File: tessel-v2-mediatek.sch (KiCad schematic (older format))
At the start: 40 parts

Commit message: swapped in power labels
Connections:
- net labels added: +1.2V, +1.8V, +3.3V
- net labels removed: +1V2, +1V8, +3V3
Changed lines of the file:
@@
-	1    0    0    -1
-$EndComp
-$Comp
-L +1V2 #PWR?
-U 1 1 548FE6C6
-P 6450 5250
-F 0 "#PWR?" H 6450 5100 60  0001 C CNN
-F 1 "+1V2" H 6450 5390 60  0000 C CNN
-F 2 "" H 6450 5250 60  0000 C CNN
-F 3 "" H 6450 5250 60  0000 C CNN
-	1    6450 5250
-	1    0    0    -1
-$EndComp
-$Comp
-L +1V8 #PWR?
-U 1 1 548FEA98
-P 7550 5250
-F 0 "#PWR?" H 7550 5100 60  0001 C CNN
-F 1 "+1V8" H 7550 5390 60  0000 C CNN
-F 2 "" H 7550 5250 60  0000 C CNN
-F 3 "" H 7550 5250 60  0000 C CNN
-	1    7550 5250
 	1    0    0    -1
 $EndComp
@@
 $EndComp
 $Comp
-L +3V3 #PWR?
+L +3.3V #PWR?
 U 1 1 548FF520
 P 8500 5350
 F 0 "#PWR?" H 8500 5200 60  0001 C CNN
-F 1 "+3V3" H 8500 5490 60  0000 C CNN
+F 1 "+3.3V" H 8500 5490 60  0000 C CNN
 F 2 "" H 8500 5350 60  0000 C CNN
 F 3 "" H 8500 5350 60  0000 C CNN
@@
 $EndComp
 $Comp
-L +3V3 #PWR?
+L +3.3V #PWR?
 U 1 1 548FF90D
 P 9450 3850
 F 0 "#PWR?" H 9450 3700 60  0001 C CNN
-F 1 "+3V3" H 9450 3990 60  0000 C CNN
+F 1 "+3.3V" H 9450 3990 60  0000 C CNN
 F 2 "" H 9450 3850 60  0000 C CNN
 F 3 "" H 9450 3850 60  0000 C CNN
@@
 Connection ~ 11200 5650
 $Comp
-L +3V3 #PWR?
+L +3.3V #PWR?
 U 1 1 54901F95
 P 11200 5100
 F 0 "#PWR?" H 11200 4950 60  0001 C CNN
-F 1 "+3V3" H 11200 5240 60  0000 C CNN
+F 1 "+3.3V" H 11200 5240 60  0000 C CNN
 F 2 "" H 11200 5100 60  0000 C CNN
 F 3 "" H 11200 5100 60  0000 C CNN
@@
 Connection ~ 7000 8350
 $Comp
-L +3V3 #PWR?
+L +3.3V #PWR?
 U 1 1 54903A33
 P 6350 8250
 F 0 "#PWR?" H 6350 8100 60  0001 C CNN
-F 1 "+3V3" H 6350 8390 60  0000 C CNN
+F 1 "+3.3V" H 6350 8390 60  0000 C CNN
 F 2 "" H 6350 8250 60  0000 C CNN
 F 3 "" H 6350 8250 60  0000 C CNN
@@
 Connection ~ 5500 8850
 Connection ~ 5150 8850
-$Comp
-L +1V8 #PWR?
-U 1 1 549048D3
-P 4800 8200
-F 0 "#PWR?" H 4800 8050 60  0001 C CNN
-F 1 "+1V8" H 4800 8340 60  0000 C CNN
-F 2 "" H 4800 8200 60  0000 C CNN
-F 3 "" H 4800 8200 60  0000 C CNN
-	1    4800 8200
-	1    0    0    -1
-$EndComp
 Wire Wire Line
 	4800 8350 4800 8200
@@
 	2150 8300 2150 8400
 Connection ~ 2400 8300
-$Comp
-L +1V2 #PWR?
-U 1 1 54905795
-P 2750 8200
-F 0 "#PWR?" H 2750 8050 60  0001 C CNN
-F 1 "+1V2" H 2750 8340 60  0000 C CNN
-F 2 "" H 2750 8200 60  0000 C CNN
-F 3 "" H 2750 8200 60  0000 C CNN
-	1    2750 8200
-	1    0    0    -1
-$EndComp
 Wire Wire Line
 	2750 8200 2750 8300
@@
 	2150 8850 7250 8850
 Connection ~ 3750 8850
+$Comp
+L +1.2V #PWR?
+U 1 1 5490938C
+P 6450 5250
+F 0 "#PWR?" H 6450 5390 20  0001 C CNN
+F 1 "+1.2V" H 6450 5360 30  0000 C CNN
+F 2 "" H 6450 5250 60  0000 C CNN
+F 3 "" H 6450 5250 60  0000 C CNN
+	1    6450 5250
+	1    0    0    -1
+$EndComp
+$Comp
+L +1.8V #PWR?
+U 1 1 549093A0
+P 7550 5250
+F 0 "#PWR?" H 7550 5390 20  0001 C CNN
+F 1 "+1.8V" H 7550 5360 30  0000 C CNN
+F 2 "" H 7550 5250 60  0000 C CNN
+F 3 "" H 7550 5250 60  0000 C CNN
+	1    7550 5250
+	1    0    0    -1
+$EndComp
+$Comp
+L +1.8V #PWR?
+U 1 1 5490A3FA
+P 4800 8200
+F 0 "#PWR?" H 4800 8340 20  0001 C CNN
+F 1 "+1.8V" H 4800 8310 30  0000 C CNN
+F 2 "" H 4800 8200 60  0000 C CNN
+F 3 "" H 4800 8200 60  0000 C CNN
+	1    4800 8200
+	1    0    0    -1
+$EndComp
+$Comp
+L +1.2V #PWR?
+U 1 1 5490A9A8
+P 2750 8200
+F 0 "#PWR?" H 2750 8340 20  0001 C CNN
+F 1 "+1.2V" H 2750 8310 30  0000 C CNN
+F 2 "" H 2750 8200 60  0000 C CNN
+F 3 "" H 2750 8200 60  0000 C CNN
+	1    2750 8200
+	1    0    0    -1
+$EndComp
 $EndSCHEMATC

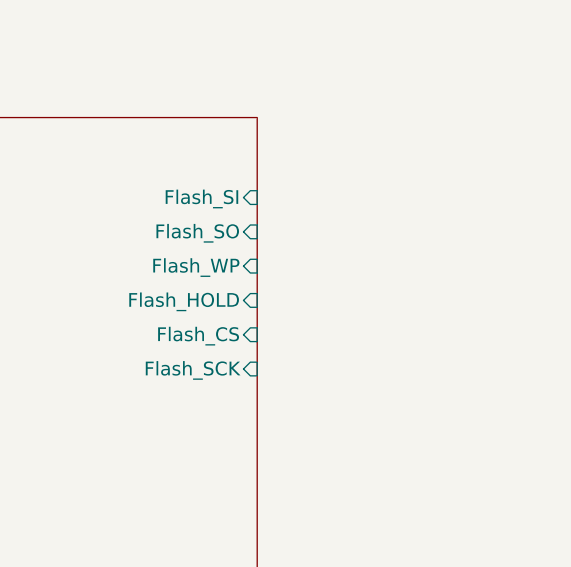
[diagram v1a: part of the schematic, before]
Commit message: adding mediatek flash labels
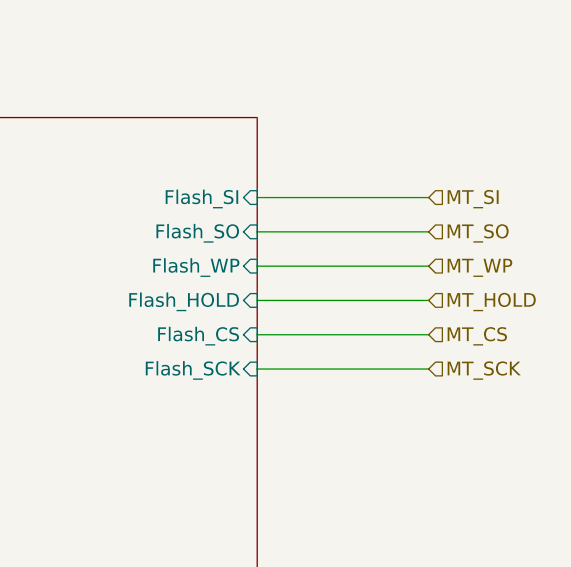
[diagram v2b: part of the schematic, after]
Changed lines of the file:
@@
 	1    0    0    -1
 $EndComp
+Text HLabel 19850 7450 2    60   Input ~ 0
+MT_SI
+Text HLabel 19850 7600 2    60   Input ~ 0
+MT_SO
+Text HLabel 19850 7750 2    60   Input ~ 0
+MT_WP
+Text HLabel 19850 7900 2    60   Input ~ 0
+MT_HOLD
+Text HLabel 19850 8050 2    60   Input ~ 0
+MT_CS
+Text HLabel 19850 8200 2    60   Input ~ 0
+MT_SCK
+Wire Wire Line
+	19100 7450 19850 7450
+Wire Wire Line
+	19100 7600 19850 7600
+Wire Wire Line
+	19100 7750 19850 7750
+Wire Wire Line
+	19100 7900 19850 7900
+Wire Wire Line
+	19100 8050 19850 8050
+Wire Wire Line
+	19100 8200 19850 8200
 $EndSCHEMATC

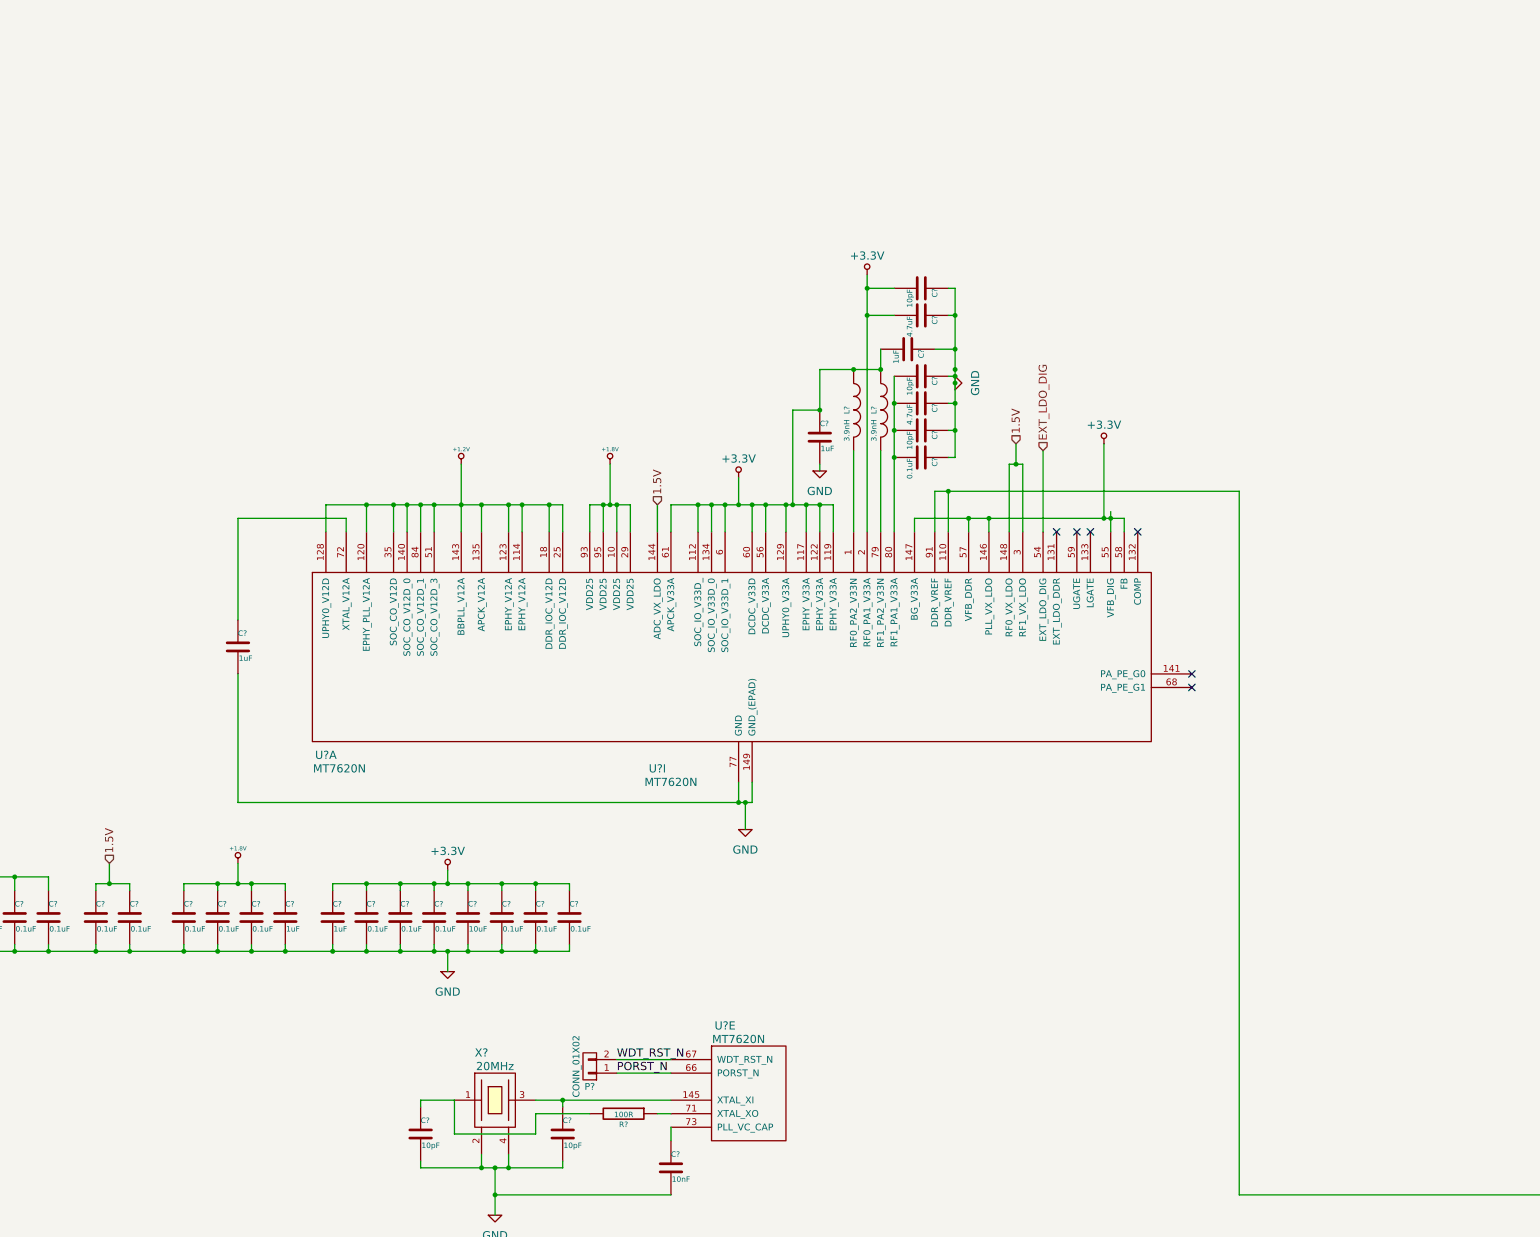
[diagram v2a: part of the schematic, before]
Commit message: cleaning up ram, rf, and mediatek power
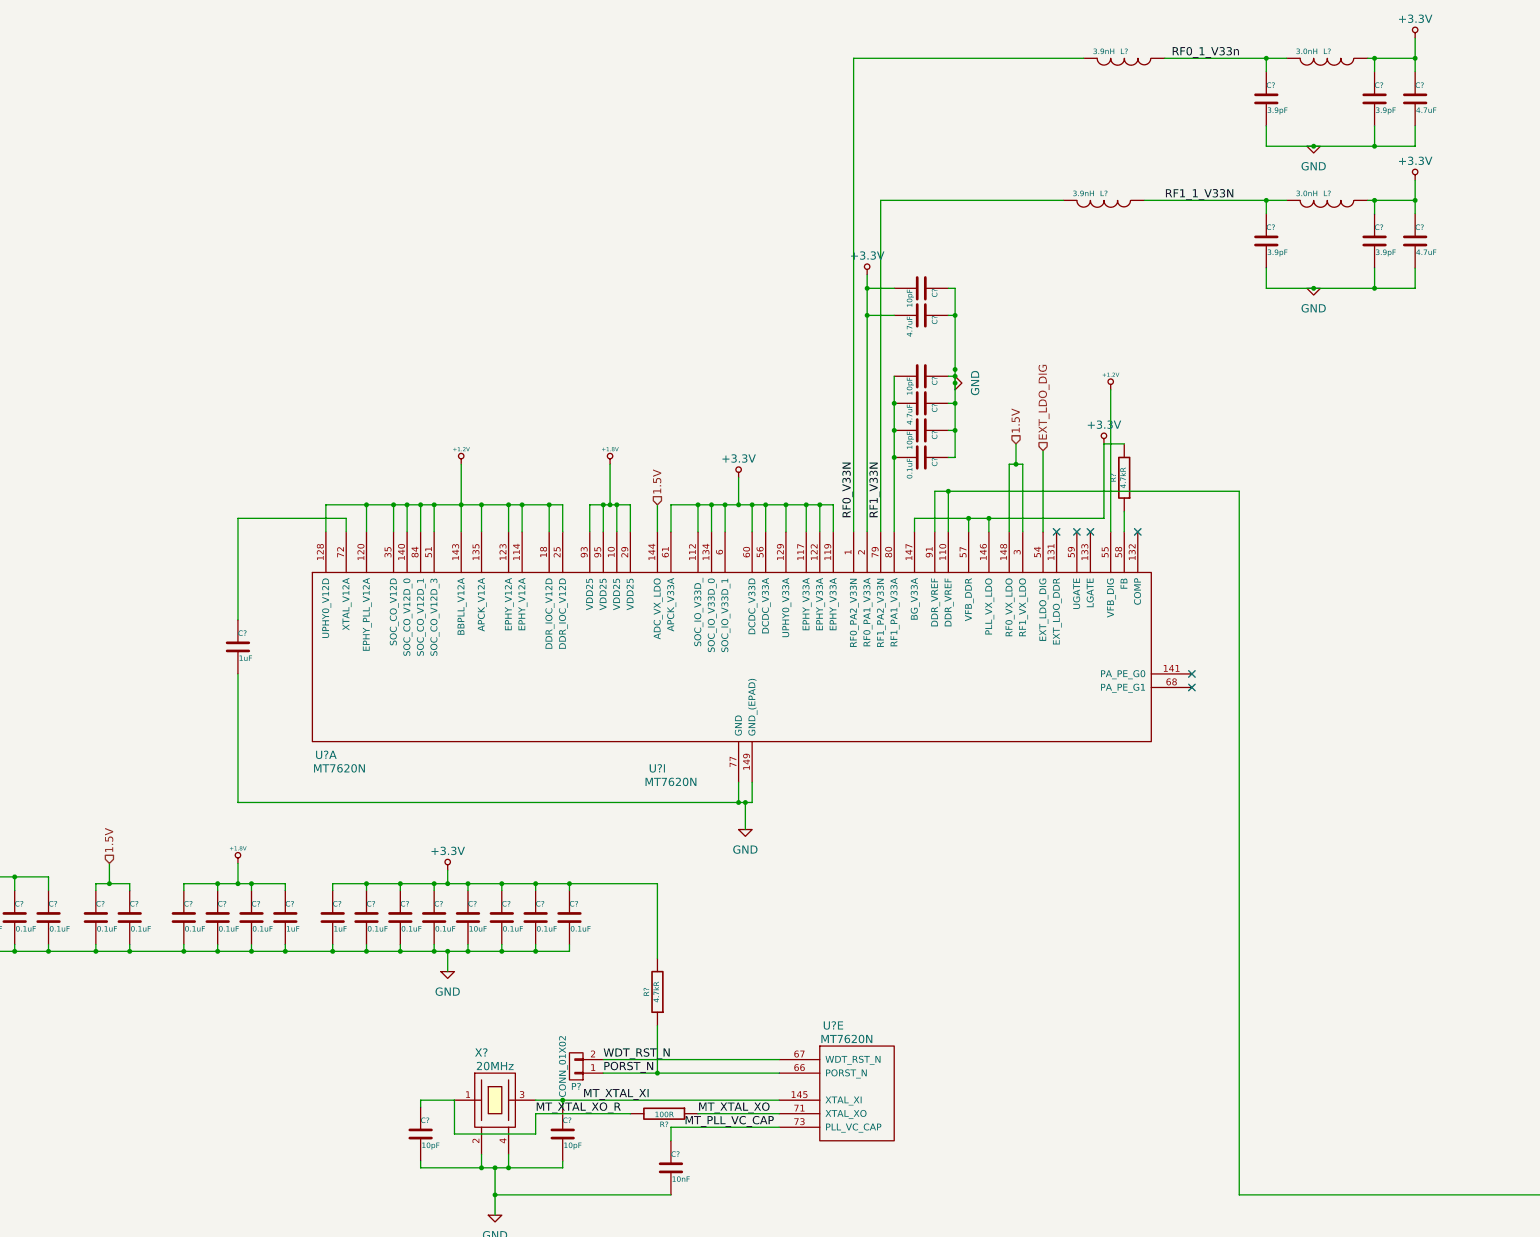
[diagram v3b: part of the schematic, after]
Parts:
- removed C?: 1uF, symbol C
- removed L?: 3.9nH, symbol INDUCTOR
- added C? (x3): 3.9pF, symbol C
- added C? (x2): 4.7uF, symbol C
- added L? (x2): 3.0nH, symbol INDUCTOR
- added L?: 3.9nH, symbol INDUCTOR
- added R? (x2): 4.7kR, symbol R
- C?: value 1uF -> 3.9pF
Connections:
- net +1.2V: now also U?.55 (VFB_DIG)
- net +3.3V: now also C?.1, C?.1, C?.1, C?.1, L?.1, L?.1, R?.2, R?.2; no longer C?.1, L?.1, U?.55 (VFB_DIG), U?.58 (FB)
- net GND: now also C?.2, C?.2, C?.2, C?.2, C?.2
- net PORST_N: now also R?.1
- net RF0_V33N: now reaches L?.2, U?.1 (RF0_PA2_V33N)
- net RF1_V33N: now reaches U?.79 (RF1_PA2_V33N)
- net RF1_V33N: now also L?.2
- net MT_XTAL_XI: now reaches C?.1, U?.145 (XTAL_XI), X?.3
- net MT_XTAL_XO: now reaches R?.1, U?.71 (XTAL_XO)
- net MT_PLL_VC_CAP: now reaches C?.1, U?.73 (PLL_VC_CAP)
- net MT_XTAL_XO_R: now reaches C?.1, R?.2, X?.1
- new net: R?.1, U?.58 (FB)
- new net RF0_1_V33n: C?.1, L?.1, L?.2
- new net RF1_1_V33N: C?.1, L?.1, L?.2
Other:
- moved on the sheet: C?, L?, P?, R?, U?E

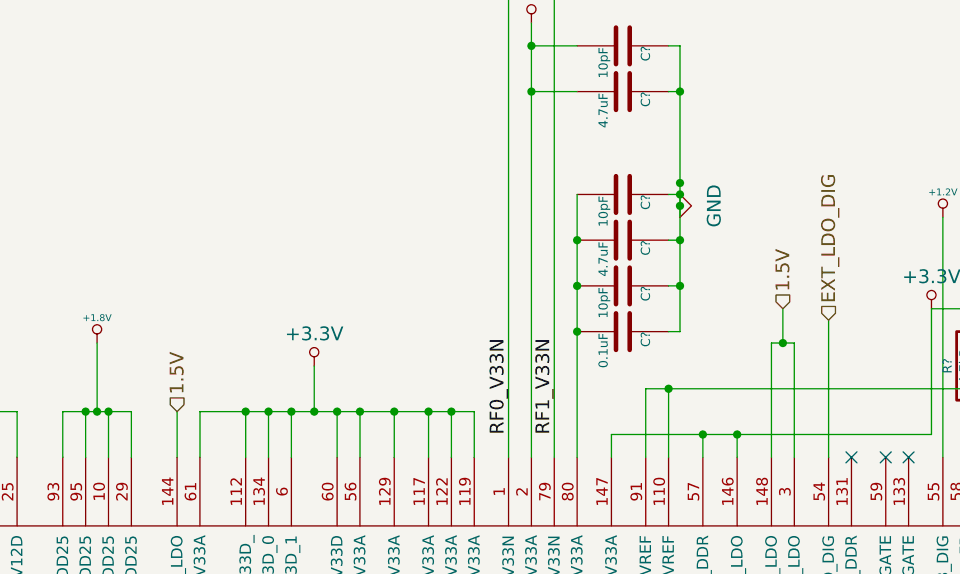
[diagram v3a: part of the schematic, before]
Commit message: setting default boot pins on rf
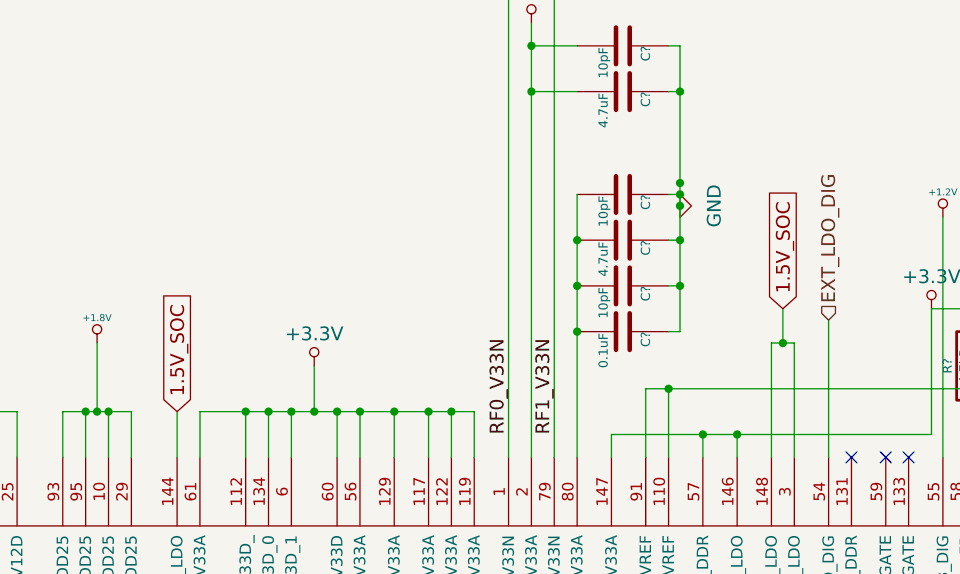
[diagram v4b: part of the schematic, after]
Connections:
- net 1.5V: no longer U?.144 (ADC_VX_LDO), U?.148 (RF0_VX_LDO), U?.3 (RF1_VX_LDO)
- new net 1.5V_SOC: U?.144 (ADC_VX_LDO), U?.148 (RF0_VX_LDO), U?.3 (RF1_VX_LDO)
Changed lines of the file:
@@
 	1    0    0    -1
 $EndComp
-Text HLabel 7900 5550 1    60   Input ~ 0
-1.5V
 $Comp
 L INDUCTOR L?
@@
 NoConn ~ 11850 6800
 NoConn ~ 11850 6900
-Text HLabel 10550 5100 1    60   Input ~ 0
-1.5V
 Text HLabel 10750 5150 1    60   Input ~ 0
 EXT_LDO_DIG
@@
 Text Label 7000 10050 0    60   ~ 0
 MT_XTAL_XO_R
+Text GLabel 7900 5550 1    60   Input ~ 0
+1.5V_SOC
+Text GLabel 10550 5100 1    60   Input ~ 0
+1.5V_SOC
 $EndSCHEMATC

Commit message: annotated
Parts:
- removed U?: MT7620N, symbol MT7620N
- gave numbers to parts that had none: 46

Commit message: give nF some love
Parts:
- C203, C204, C205, C206, C207, C208, C209, C210, C212, C215, C216, C218, C220, C221, C223, C230: value 0.1uF -> 100nF
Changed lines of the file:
@@
 P 11350 2250
 F 0 "L202" V 11300 2250 40  0000 C CNN
-F 1 "3.9nH" V 11300 2100 40  0000 C CNN
+F 1 "3.9nH" V 11450 2250 40  0000 C CNN
 F 2 "" H 11350 2250 60  0000 C CNN
 F 3 "" H 11350 2250 60  0000 C CNN
@@
 P 9850 5200
 F 0 "C230" H 9850 5300 40  0000 L CNN
-F 1 "0.1uF" H 9856 5115 40  0000 L CNN
+F 1 "100nF" H 9856 5115 40  0000 L CNN
 F 2 "" H 9888 5050 30  0000 C CNN
 F 3 "" H 9850 5200 60  0000 C CNN
@@
 P 5750 8600
 F 0 "C215" H 5750 8700 40  0000 L CNN
-F 1 "0.1uF" H 5756 8515 40  0000 L CNN
+F 1 "100nF" H 5756 8515 40  0000 L CNN
 F 2 "" H 5788 8450 30  0000 C CNN
 F 3 "" H 5750 8600 60  0000 C CNN
@@
 P 6000 8600
 F 0 "C216" H 6000 8700 40  0000 L CNN
-F 1 "0.1uF" H 6006 8515 40  0000 L CNN
+F 1 "100nF" H 6006 8515 40  0000 L CNN
 F 2 "" H 6038 8450 30  0000 C CNN
 F 3 "" H 6000 8600 60  0000 C CNN
@@
 P 6250 8600
 F 0 "C218" H 6250 8700 40  0000 L CNN
-F 1 "0.1uF" H 6256 8515 40  0000 L CNN
+F 1 "100nF" H 6256 8515 40  0000 L CNN
 F 2 "" H 6288 8450 30  0000 C CNN
 F 3 "" H 6250 8600 60  0000 C CNN
@@
 P 6750 8600
 F 0 "C220" H 6750 8700 40  0000 L CNN
-F 1 "0.1uF" H 6756 8515 40  0000 L CNN
+F 1 "100nF" H 6756 8515 40  0000 L CNN
 F 2 "" H 6788 8450 30  0000 C CNN
 F 3 "" H 6750 8600 60  0000 C CNN
@@
 P 7000 8600
 F 0 "C221" H 7000 8700 40  0000 L CNN
-F 1 "0.1uF" H 7006 8515 40  0000 L CNN
+F 1 "100nF" H 7006 8515 40  0000 L CNN
 F 2 "" H 7038 8450 30  0000 C CNN
 F 3 "" H 7000 8600 60  0000 C CNN
@@
 P 7250 8600
 F 0 "C223" H 7250 8700 40  0000 L CNN
-F 1 "0.1uF" H 7256 8515 40  0000 L CNN
+F 1 "100nF" H 7256 8515 40  0000 L CNN
 F 2 "" H 7288 8450 30  0000 C CNN
 F 3 "" H 7250 8600 60  0000 C CNN
@@
 P 4400 8600
 F 0 "C209" H 4400 8700 40  0000 L CNN
-F 1 "0.1uF" H 4406 8515 40  0000 L CNN
+F 1 "100nF" H 4406 8515 40  0000 L CNN
 F 2 "" H 4438 8450 30  0000 C CNN
 F 3 "" H 4400 8600 60  0000 C CNN
@@
 P 4650 8600
 F 0 "C210" H 4650 8700 40  0000 L CNN
-F 1 "0.1uF" H 4656 8515 40  0000 L CNN
+F 1 "100nF" H 4656 8515 40  0000 L CNN
 F 2 "" H 4688 8450 30  0000 C CNN
 F 3 "" H 4650 8600 60  0000 C CNN
@@
 P 4900 8600
 F 0 "C212" H 4900 8700 40  0000 L CNN
-F 1 "0.1uF" H 4906 8515 40  0000 L CNN
+F 1 "100nF" H 4906 8515 40  0000 L CNN
 F 2 "" H 4938 8450 30  0000 C CNN
 F 3 "" H 4900 8600 60  0000 C CNN
@@
 P 3400 8600
 F 0 "C206" H 3400 8700 40  0000 L CNN
-F 1 "0.1uF" H 3406 8515 40  0000 L CNN
+F 1 "100nF" H 3406 8515 40  0000 L CNN
 F 2 "" H 3438 8450 30  0000 C CNN
 F 3 "" H 3400 8600 60  0000 C CNN
@@
 P 3150 8600
 F 0 "C205" H 3150 8700 40  0000 L CNN
-F 1 "0.1uF" H 3156 8515 40  0000 L CNN
+F 1 "100nF" H 3156 8515 40  0000 L CNN
 F 2 "" H 3188 8450 30  0000 C CNN
 F 3 "" H 3150 8600 60  0000 C CNN
@@
 P 2900 8600
 F 0 "C204" H 2900 8700 40  0000 L CNN
-F 1 "0.1uF" H 2906 8515 40  0000 L CNN
+F 1 "100nF" H 2906 8515 40  0000 L CNN
 F 2 "" H 2938 8450 30  0000 C CNN
 F 3 "" H 2900 8600 60  0000 C CNN
@@
 P 2650 8600
 F 0 "C203" H 2650 8700 40  0000 L CNN
-F 1 "0.1uF" H 2656 8515 40  0000 L CNN
+F 1 "100nF" H 2656 8515 40  0000 L CNN
 F 2 "" H 2688 8450 30  0000 C CNN
 F 3 "" H 2650 8600 60  0000 C CNN
@@
 P 3750 8600
 F 0 "C207" H 3750 8700 40  0000 L CNN
-F 1 "0.1uF" H 3756 8515 40  0000 L CNN
+F 1 "100nF" H 3756 8515 40  0000 L CNN
 F 2 "" H 3788 8450 30  0000 C CNN
 F 3 "" H 3750 8600 60  0000 C CNN
@@
 P 4000 8600
 F 0 "C208" H 4000 8700 40  0000 L CNN
-F 1 "0.1uF" H 4006 8515 40  0000 L CNN
+F 1 "100nF" H 4006 8515 40  0000 L CNN
 F 2 "" H 4038 8450 30  0000 C CNN
 F 3 "" H 4000 8600 60  0000 C CNN
@@
 P 12850 2250
 F 0 "L203" V 12800 2250 40  0000 C CNN
-F 1 "3.0nH" V 12800 2100 40  0000 C CNN
+F 1 "3.0nH" V 12950 2250 40  0000 C CNN
 F 2 "" H 12850 2250 60  0000 C CNN
 F 3 "" H 12850 2250 60  0000 C CNN
@@
 P 11200 3300
 F 0 "L201" V 11150 3300 40  0000 C CNN
-F 1 "3.9nH" V 11150 3150 40  0000 C CNN
+F 1 "3.9nH" V 11300 3300 40  0000 C CNN
 F 2 "" H 11200 3300 60  0000 C CNN
 F 3 "" H 11200 3300 60  0000 C CNN
@@
 P 12850 3300
 F 0 "L204" V 12800 3300 40  0000 C CNN
-F 1 "3.0nH" V 12800 3150 40  0000 C CNN
+F 1 "3.0nH" V 12950 3300 40  0000 C CNN
 F 2 "" H 12850 3300 60  0000 C CNN
 F 3 "" H 12850 3300 60  0000 C CNN

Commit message: second pass schem check
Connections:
- net 1.5V is gone; now on net 1.5V_SOC: C207.1, C208.1
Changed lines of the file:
@@
 	1    0    0    -1
 $EndComp
-Text HLabel 3850 8200 1    60   Input ~ 0
-1.5V
 $Comp
 L +1.2V #PWR205
@@
 Text GLabel 10550 5100 1    60   Input ~ 0
 1.5V_SOC
+Text GLabel 3850 8200 1    60   Input ~ 0
+1.5V_SOC
 $EndSCHEMATC
